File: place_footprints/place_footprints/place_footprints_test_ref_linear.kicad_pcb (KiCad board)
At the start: 2 copper layers, 64 parts

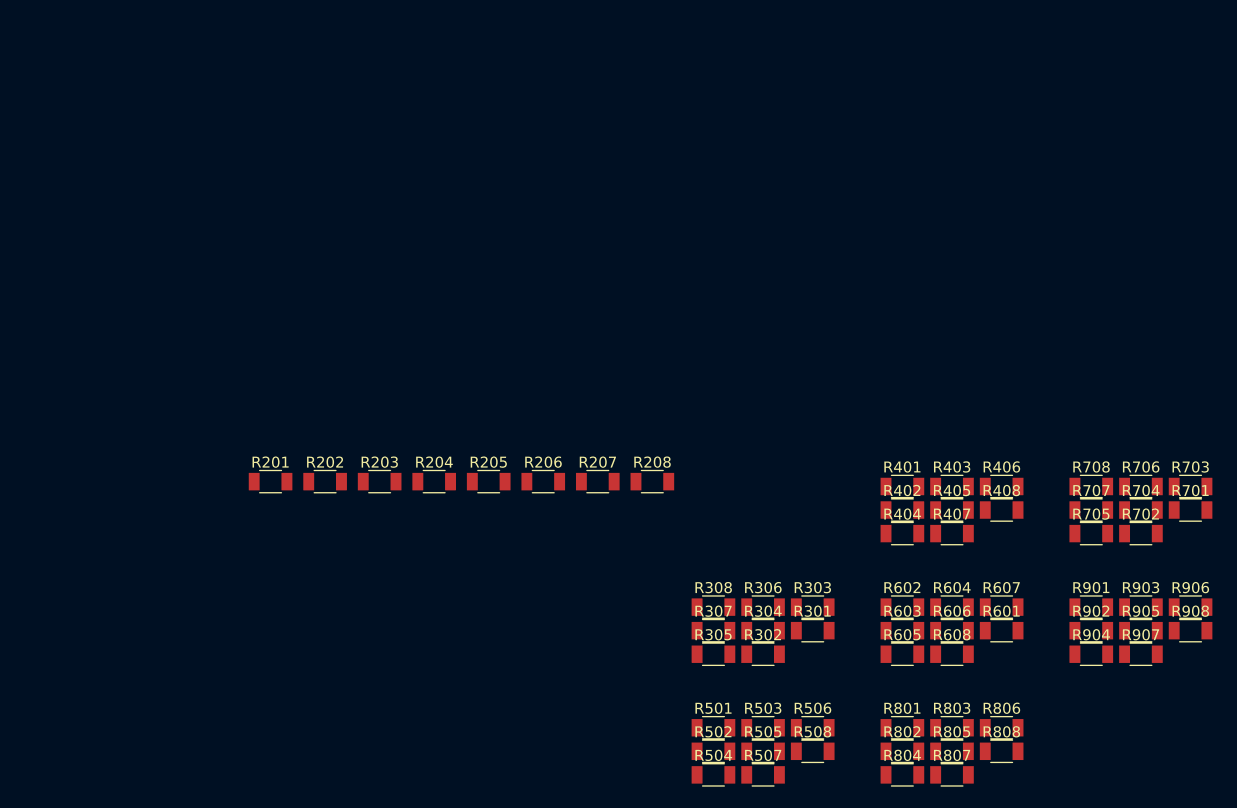
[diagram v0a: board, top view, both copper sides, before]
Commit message: Fixed circular placement
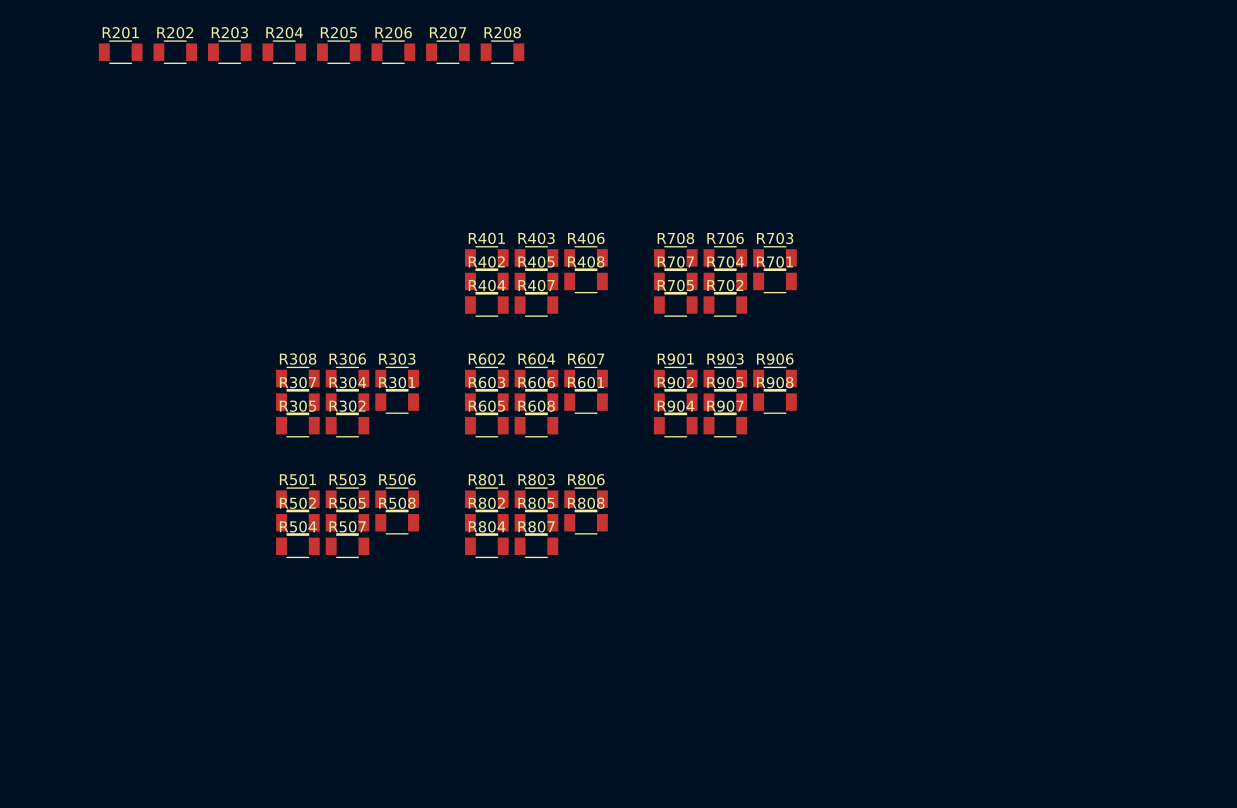
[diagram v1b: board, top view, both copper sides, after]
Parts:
- moved R301 43.5 mm to (69.2, 61.3)
- moved R302 43.5 mm to (64.6, 63.5)
- moved R303 43.5 mm to (69.2, 59.1)
- moved R304 43.5 mm to (64.6, 61.3)
- moved R306 43.5 mm to (64.6, 59.1)
- moved R401 43.5 mm to (77.4, 48.1)
- moved R402 43.5 mm to (77.4, 50.2)
- moved R404 43.5 mm to (77.4, 52.4)
- moved R503 43.5 mm to (64.6, 70.2)
- moved R505 43.5 mm to (64.6, 72.4)
- moved R506 43.5 mm to (69.2, 70.2)
- moved R507 43.5 mm to (64.6, 74.5)
- moved R508 43.5 mm to (69.2, 72.4)
- moved R602 43.5 mm to (77.4, 59.1)
- moved R603 43.5 mm to (77.4, 61.3)
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
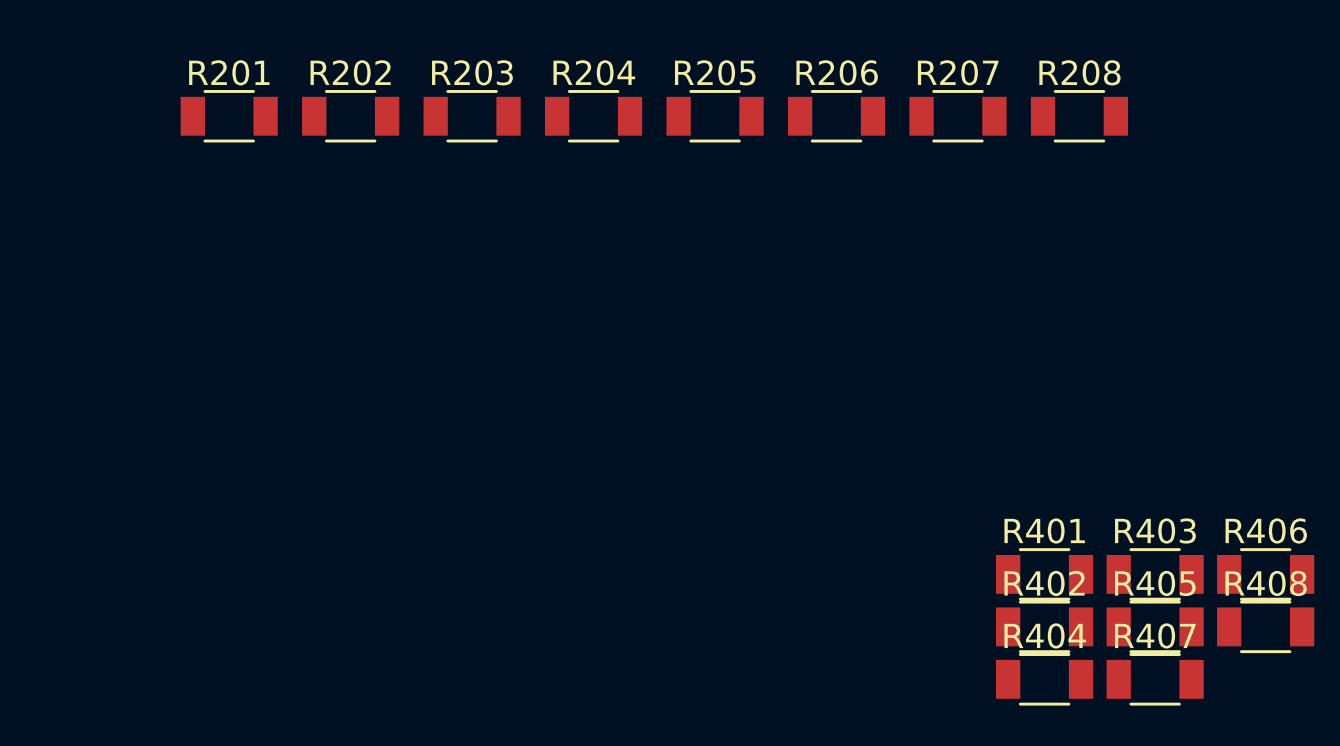
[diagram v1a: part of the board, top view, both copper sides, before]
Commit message: added support for any footprint to serve as a reference in linear and circular mode
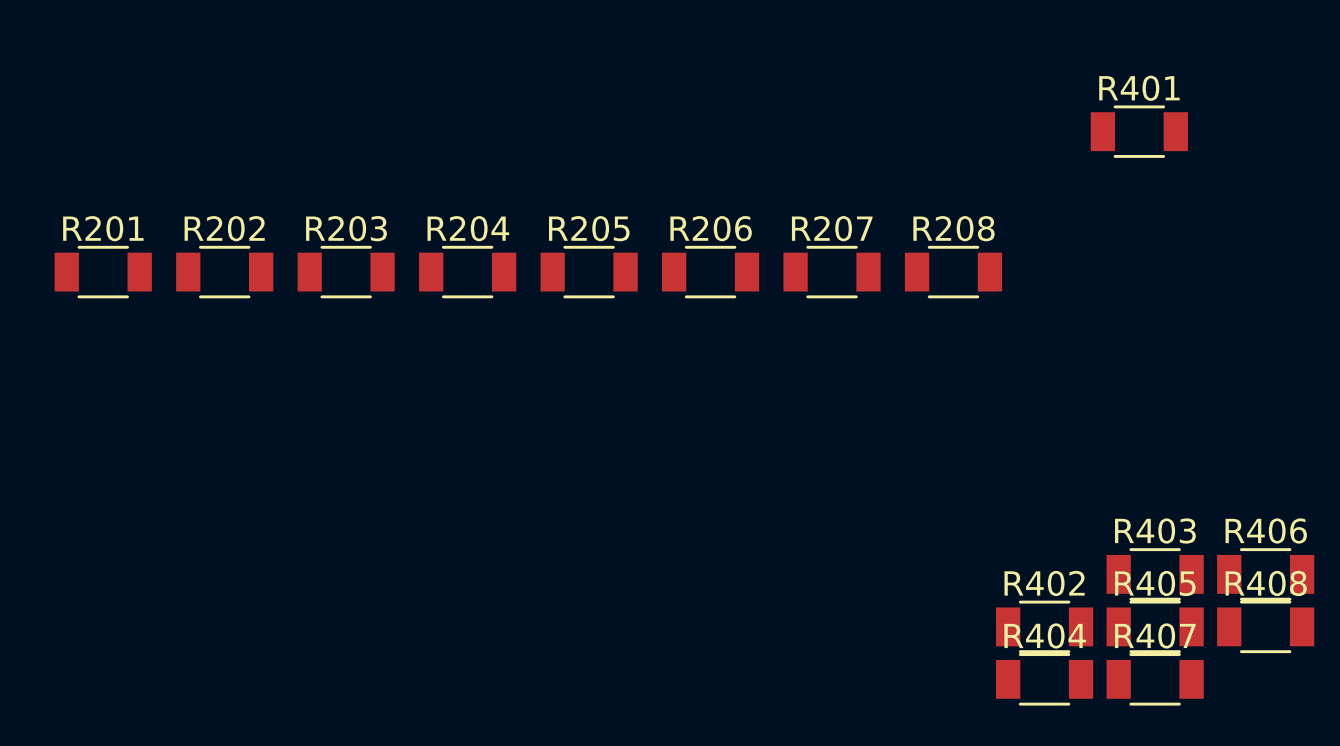
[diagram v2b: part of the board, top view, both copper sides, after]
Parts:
- moved R401 18.6 mm to (81.3, 29.8)
- moved R207 8.25 mm to (68.6, 35.6)
- moved R208 8.25 mm to (73.6, 35.6)
- moved R201 8.25 mm to (38.6, 35.6)
- moved R202 8.25 mm to (43.6, 35.6)
- moved R203 8.25 mm to (48.6, 35.6)
- moved R204 8.25 mm to (53.6, 35.6)
- moved R205 8.25 mm to (58.6, 35.6)
- moved R206 8.25 mm to (63.6, 35.6)
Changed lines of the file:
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@@
-(kicad_pcb (version 20171130) (host pcbnew "(5.0.2)-1")
+(kicad_pcb (version 20171130) (host pcbnew "(5.1.0-rc2-4-g73f0b3087)")
   (general
     (thickness 1.6)
@@
     (zone_45_only no)
     (trace_min 0.2)
-    (segment_width 0.2)
-    (edge_width 0.15)
     (via_size 0.8)
     (via_drill 0.4)
@@
     (uvia_min_size 0.2)
     (uvia_min_drill 0.1)
+    (edge_width 0.15)
+    (segment_width 0.2)
     (pcb_text_width 0.3)
     (pcb_text_size 1.5 1.5)
@@
   )
   (module Passives:R1206M (layer F.Cu)
-    (at 43.815 29.21)
+    (at 38.630001 35.625001)
     (descr "Capacitor SMD 1206, reflow soldering, AVX (see smccp.pdf)")
     (tags "capacitor 1206")
@@
   )
   (module Passives:R1206M (layer F.Cu)
-    (at 78.815 29.21)
+    (at 73.630001 35.625001)
     (descr "Capacitor SMD 1206, reflow soldering, AVX (see smccp.pdf)")
     (tags "capacitor 1206")
@@
   )
   (module Passives:R1206M (layer F.Cu)
-    (at 73.815 29.21)
+    (at 68.630001 35.625001)
     (descr "Capacitor SMD 1206, reflow soldering, AVX (see smccp.pdf)")
     (tags "capacitor 1206")
@@
   )
   (module Passives:R1206M (layer F.Cu)
-    (at 68.815 29.21)
+    (at 63.630001 35.625001)
     (descr "Capacitor SMD 1206, reflow soldering, AVX (see smccp.pdf)")
     (tags "capacitor 1206")
@@
   )
   (module Passives:R1206M (layer F.Cu)
-    (at 63.815 29.21)
+    (at 58.630001 35.625001)
     (descr "Capacitor SMD 1206, reflow soldering, AVX (see smccp.pdf)")
     (tags "capacitor 1206")
@@
   )
   (module Passives:R1206M (layer F.Cu)
-    (at 58.815 29.21)
+    (at 53.630001 35.625001)
     (descr "Capacitor SMD 1206, reflow soldering, AVX (see smccp.pdf)")
     (tags "capacitor 1206")
@@
   )
   (module Passives:R1206M (layer F.Cu)
-    (at 53.815 29.21)
+    (at 48.630001 35.625001)
     (descr "Capacitor SMD 1206, reflow soldering, AVX (see smccp.pdf)")
     (tags "capacitor 1206")
@@
   )
   (module Passives:R1206M (layer F.Cu)
-    (at 48.815 29.21)
+    (at 43.630001 35.625001)
     (descr "Capacitor SMD 1206, reflow soldering, AVX (see smccp.pdf)")
     (tags "capacitor 1206")
@@
   )
   (module Passives:R1206M (layer F.Cu)
-    (at 77.380001 48.070001)
-    (descr "Capacitor SMD 1206, reflow soldering, AVX (see smccp.pdf)")
-    (tags "capacitor 1206")
+    (at 81.28 29.845)
+    (descr "Capacitor SMD 1206, reflow soldering, AVX (see smccp.pdf)")
+    (tags "capacitor 1206")

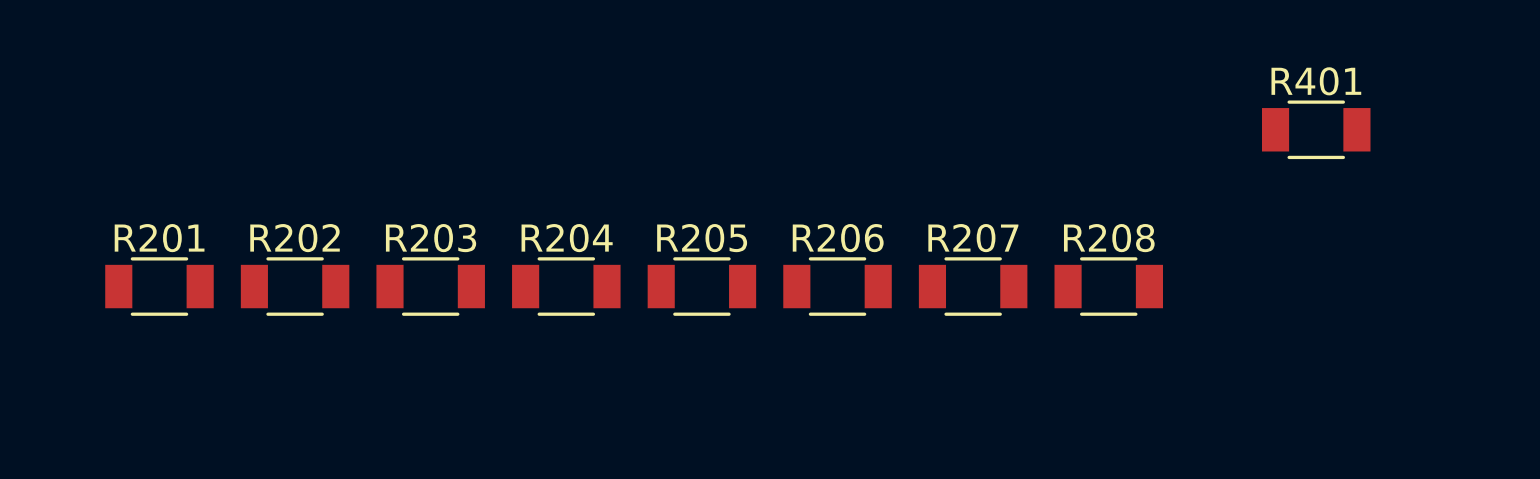
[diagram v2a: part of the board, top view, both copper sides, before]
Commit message: updated test cases
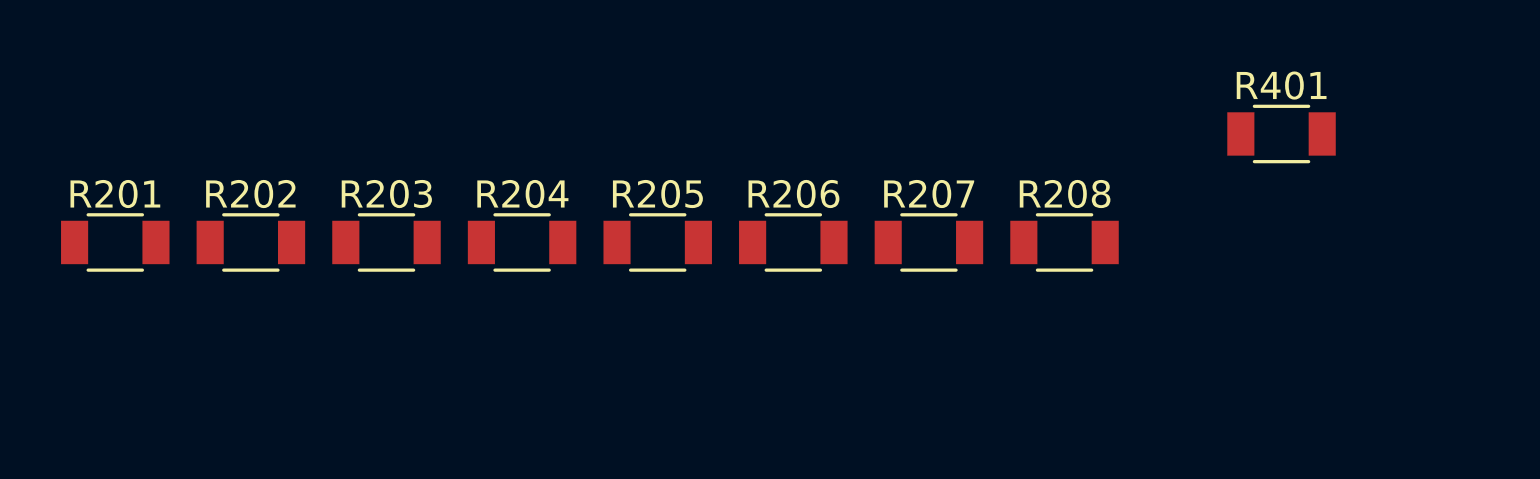
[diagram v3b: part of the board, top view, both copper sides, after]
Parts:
- moved R201 2.30 mm to (37.0, 34.0)
- moved R202 2.30 mm to (42.0, 34.0)
- moved R203 2.30 mm to (47.0, 34.0)
- moved R204 2.30 mm to (52.0, 34.0)
- moved R205 2.30 mm to (57.0, 34.0)
- moved R206 2.30 mm to (62.0, 34.0)
- moved R207 2.30 mm to (67.0, 34.0)
- moved R208 2.30 mm to (72.0, 34.0)
- moved R401 1.29 mm to (80.0, 30.0)
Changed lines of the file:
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@@
-(kicad_pcb (version 20171130) (host pcbnew "(5.1.0-rc2-4-g73f0b3087)")
+(kicad_pcb (version 20171130) (host pcbnew "(5.1.5-90-g5c7ac1bb7)-1")
   (general
     (thickness 1.6)
@@
   )
   (module Passives:R1206M (layer F.Cu)
-    (at 38.630001 35.625001)
+    (at 37 34)
     (descr "Capacitor SMD 1206, reflow soldering, AVX (see smccp.pdf)")
     (tags "capacitor 1206")
@@
   )
   (module Passives:R1206M (layer F.Cu)
-    (at 73.630001 35.625001)
+    (at 72 34)
     (descr "Capacitor SMD 1206, reflow soldering, AVX (see smccp.pdf)")
     (tags "capacitor 1206")
@@
   )
   (module Passives:R1206M (layer F.Cu)
-    (at 68.630001 35.625001)
+    (at 67 34)
     (descr "Capacitor SMD 1206, reflow soldering, AVX (see smccp.pdf)")
     (tags "capacitor 1206")
@@
   )
   (module Passives:R1206M (layer F.Cu)
-    (at 63.630001 35.625001)
+    (at 62 34)
     (descr "Capacitor SMD 1206, reflow soldering, AVX (see smccp.pdf)")
     (tags "capacitor 1206")
@@
   )
   (module Passives:R1206M (layer F.Cu)
-    (at 58.630001 35.625001)
+    (at 57 34)
     (descr "Capacitor SMD 1206, reflow soldering, AVX (see smccp.pdf)")
     (tags "capacitor 1206")
@@
   )
   (module Passives:R1206M (layer F.Cu)
-    (at 53.630001 35.625001)
+    (at 52 34)
     (descr "Capacitor SMD 1206, reflow soldering, AVX (see smccp.pdf)")
     (tags "capacitor 1206")
@@
   )
   (module Passives:R1206M (layer F.Cu)
-    (at 48.630001 35.625001)
+    (at 47 34)
     (descr "Capacitor SMD 1206, reflow soldering, AVX (see smccp.pdf)")
     (tags "capacitor 1206")
@@
   )
   (module Passives:R1206M (layer F.Cu)
-    (at 43.630001 35.625001)
+    (at 42 34)
     (descr "Capacitor SMD 1206, reflow soldering, AVX (see smccp.pdf)")
     (tags "capacitor 1206")
@@
   )
   (module Passives:R1206M (layer F.Cu)
-    (at 81.28 29.845)
-    (descr "Capacitor SMD 1206, reflow soldering, AVX (see smccp.pdf)")
-    (tags "capacitor 1206")
+    (at 80 30)
+    (descr "Capacitor SMD 1206, reflow soldering, AVX (see smccp.pdf)")
+    (tags "capacitor 1206")
